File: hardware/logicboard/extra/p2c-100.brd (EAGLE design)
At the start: 91 x 55 mm, 49 parts, among them IC1 74LS07N, K1 G5V1, T1 2SC1815, U1 MKR1000

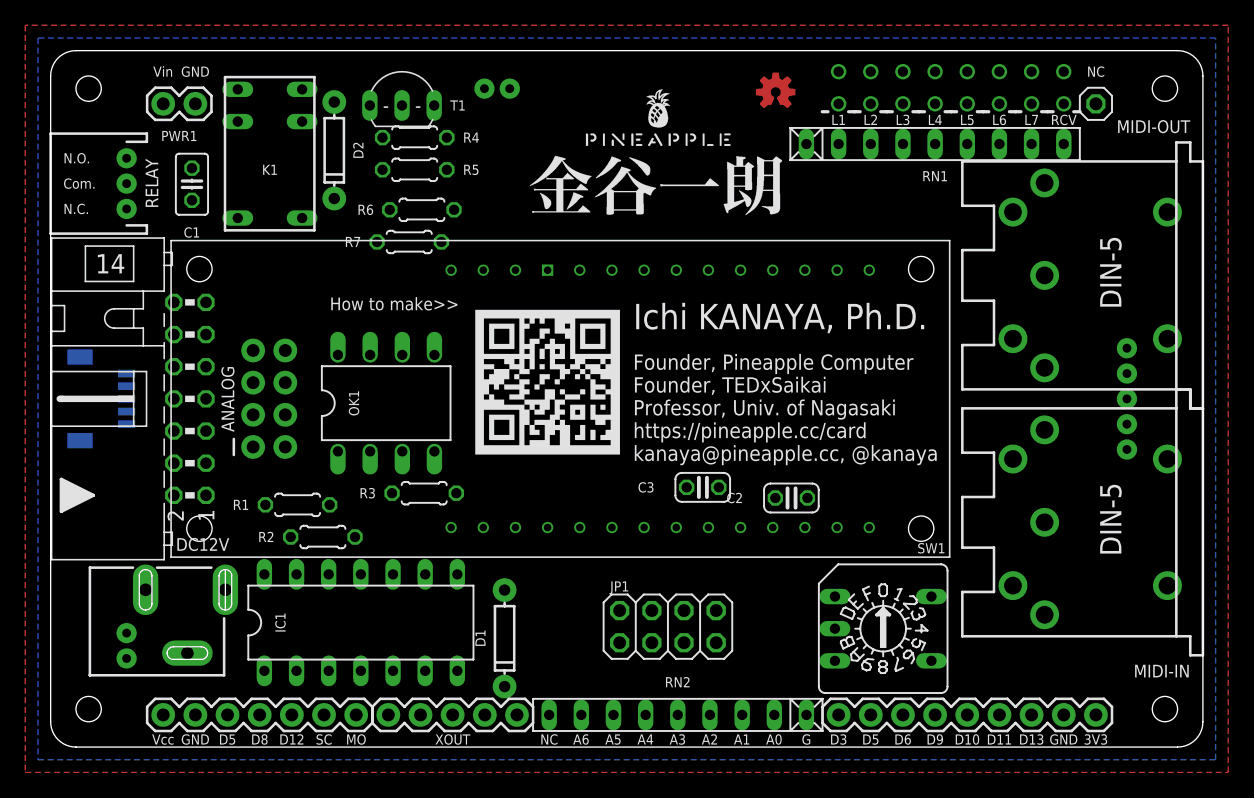
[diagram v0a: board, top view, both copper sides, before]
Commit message: Test of MKR1000 version.
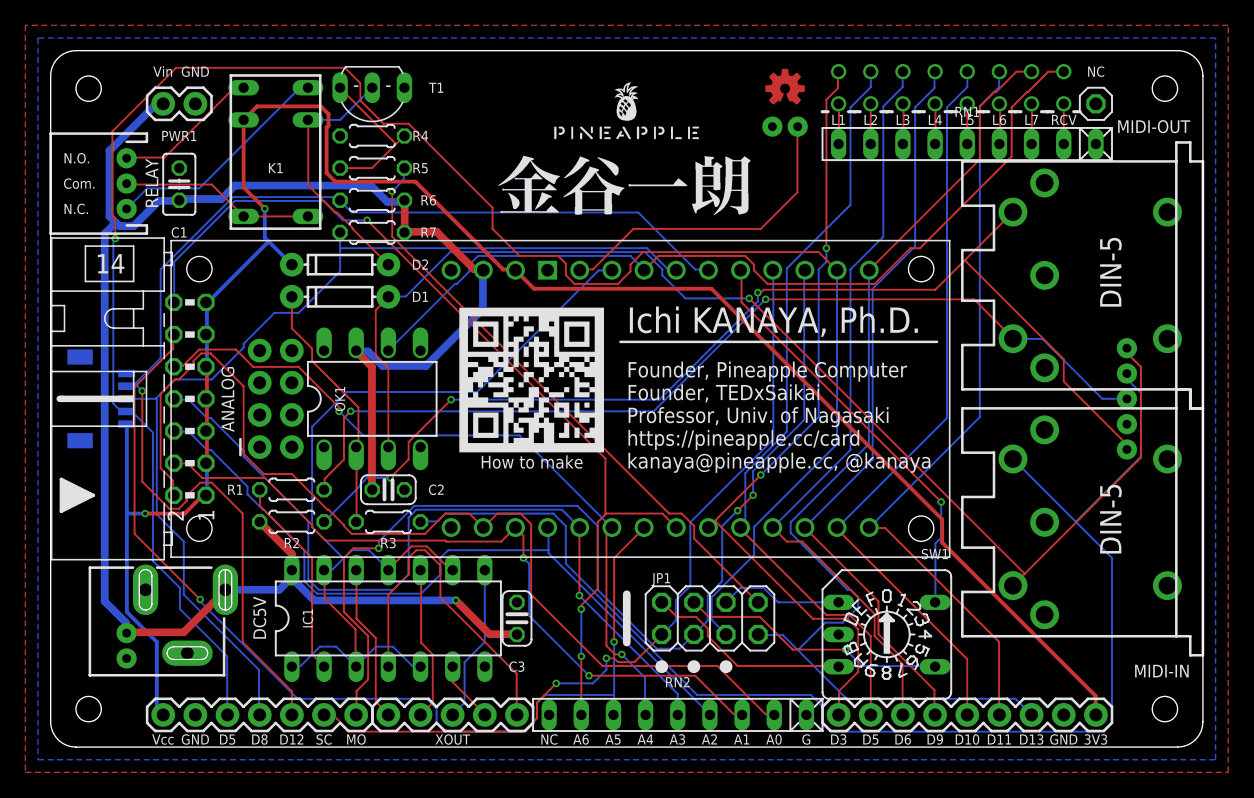
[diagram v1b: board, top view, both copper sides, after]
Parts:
- moved C2 31.8 mm to (26.7, 20.3)
- moved D1 29.9 mm to (22.9, 35.6), turned to 180 degrees
- moved RST 22.9 mm to (58.0, 49.0)
- moved C3 18.0 mm to (36.8, 10.2), turned to 90 degrees
- moved D2 9.04 mm to (22.9, 38.1), turned to 180 degrees
- moved R6 3.99 mm to (25.4, 43.2)
- moved R3 3.63 mm to (26.7, 17.8)
- moved JP1 3.38 mm to (52.1, 10.2)
- moved R4 3.35 mm to (25.4, 48.3)
- moved R5 3.35 mm to (25.4, 45.7)
- moved R7 3.01 mm to (25.4, 40.6)
- moved T1 2.74 mm to (25.4, 52.1), turned to 180 degrees
- moved R2 2.72 mm to (19.1, 17.8)
- moved U$1 2.56 mm to (45.5, 48.0)
- moved RN1 2.54 mm to (72.4, 47.6), turned to 180 degrees
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- renumbered DC12V to DC5V
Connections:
- net X1 renamed XOUT_1
- net X2 renamed XOUT_2
- net X3 renamed XOUT_3
- net X4 renamed XOUT_4
- net X5 renamed XOUT_5
- removed net ANLG_0: ANALOG.2, RN2.2
- removed net ANLG_1: ANALOG.4, RN2.3
- removed net ANLG_2: ANALOG.6, RN2.4
- removed net ANLG_3: ANALOG.8, RN2.5
- removed net ANLG_4: ANALOG.10, RN2.6
- removed net ANLG_5: ANALOG.12, RN2.7
- removed net ANLG_6: ANALOG.14, RN2.8
- removed net LED1K: L1.K, RN1.2
- removed net LED2K: L2.K, RN1.3
- removed net LED3K: L3.K, RN1.4
- removed net LED4K: L4.K, RN1.5
- removed net LED5K: L5.K, RN1.6
- removed net LED6K: L6.K, RN1.7
- removed net LED7K: L7.K, RN1.8
- removed net MIDIIN: OK1.6, RCV.A
- removed net MIDIOUT: IC1.1, IC1.11, IC1.13, IC1.3, IC1.5, IC1.9
- removed net PWM_0: DIGITAL.9, L1.A
- removed net PWM_1: DIGITAL.8, L2.A
- removed net PWM_2: DIGITAL.7, L3.A
- removed net PWM_3: DIGITAL.6, L4.A
- removed net PWM_4: DIGITAL.5, L5.A
- removed net PWM_5: DIGITAL.4, L6.A
- removed net PWM_6: DIGITAL.3, L7.A
- removed net RLYDRV: JP1.7, R5.2
- removed net VIN: DC5V.PWR, PWR1.1, PWR2.1, U1.VIN
- new net ANALOG_0: ANALOG.2, RN2.2, U1.A0
- new net ANALOG_1: ANALOG.4, RN2.3, U1.A1
- new net ANALOG_2: ANALOG.6, RN2.4, U1.A2
- new net ANALOG_3: ANALOG.8, RN2.5, U1.A3
- new net ANALOG_4: ANALOG.10, RN2.6, U1.A4
- new net ANALOG_5: ANALOG.12, RN2.7, U1.A5
- new net ANALOG_6: ANALOG.14, RN2.8, U1.A6
- new net DIGITAL_0: DIGITAL.9, L1.A, U1.D0
- new net DIGITAL_1: DIGITAL.8, L2.A, U1.D1
- new net DIGITAL_10: SW1.8, U1.D10
- new net DIGITAL_11: I2C.4, LIGHTDRIVE.5, R6.1, U1.D11
- new net DIGITAL_12: I2C.3, LIGHTDRIVE.4, R7.1, U1.D12
- new net DIGITAL_13: OK1.6, RCV.A, U1.D13
- new net DIGITAL_14: IC1.1, IC1.11, IC1.13, IC1.3, IC1.5, IC1.9, U1.D14
- new net DIGITAL_2: DIGITAL.7, L3.A, U1.D2
- new net DIGITAL_3: DIGITAL.6, L4.A, U1.D3
- new net DIGITAL_4: DIGITAL.5, L5.A, U1.D4
- new net DIGITAL_5: DIGITAL.4, L6.A, U1.D5
- new net DIGITAL_6: DIGITAL.3, JP1.7, L7.A, U1.D6
- new net DIGITAL_7: I2C.2, JP1.5, LIGHTDRIVE.3, U1.D7
- new net DIGITAL_8: JP1.3, LIGHTDRIVE.7, U1.D8
- new net DIGITAL_9: JP1.1, LIGHTDRIVE.6, U1.D9
- new net N$10: L5.K, RN1.5
- new net N$11: L6.K, RN1.4
- new net N$12: L7.K, RN1.3
- new net N$13: RCV.K, RN1.2
- new net N$2: RST.1, U1.RST
- new net N$3: JP1.8, R5.2
- new net N$4: JP1.6, SW1.1
- new net N$5: JP1.4, SW1.2
- new net N$6: JP1.2, SW1.4
- new net N$7: L2.K, RN1.8
- new net N$8: L3.K, RN1.7
- new net N$9: L4.K, RN1.6
- net GND: no longer DIGITAL.2, JP1.1
- net N$1: now also L1.K; no longer RCV.K
- net VCC: now also DC5V.PWR, PWR1.1, PWR2.1, U1.VIN; no longer ANALOG.1, ANALOG.11, ANALOG.13, ANALOG.3, ANALOG.5, ANALOG.7, ANALOG.9, D2.C, K1.2, LIGHTDRIVE.1
- net VDD: now also ANALOG.1, ANALOG.11, ANALOG.13, ANALOG.3, ANALOG.5, ANALOG.7, ANALOG.9, D2.C, K1.2, LIGHTDRIVE.1, U1.3V3
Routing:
- net VDD: track 0.00 -> 159.2 mm, vias 0 -> 2
- net DIGITAL_7: track 0.00 -> 154.5 mm, vias 0 -> 1
- net VCC: track 0.00 -> 147.5 mm, vias 0 -> 1
- net MIDIIN+: track 0.00 -> 103.1 mm
- net MIDIIN-: track 0.00 -> 98.6 mm, vias 0 -> 1
- net DIGITAL_11: track 0.00 -> 95.1 mm, vias 0 -> 1
- net MIDIOUT+: track 0.00 -> 86.0 mm, vias 0 -> 3
- net DIGITAL_8: track 0.00 -> 83.7 mm, vias 0 -> 3
- net DIGITAL_6: track 0.00 -> 83.7 mm
- net DIGITAL_12: track 0.00 -> 79.9 mm
- net ANALOG_5: track 0.00 -> 79.8 mm, vias 0 -> 2
- net ANALOG_0: track 0.00 -> 79.0 mm
- net MIDIOUT-: track 0.00 -> 75.3 mm, vias 0 -> 2
- net DIGITAL_14: track 0.00 -> 74.8 mm
- net ANALOG_6: track 0.00 -> 74.8 mm, vias 0 -> 3
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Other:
- board text added: "How to make"
- board text removed: "How to make>>"
